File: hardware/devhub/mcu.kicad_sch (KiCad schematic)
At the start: 18 parts, among them J4 SWD, J9 UART debug, U3 STM32G0B1RET6

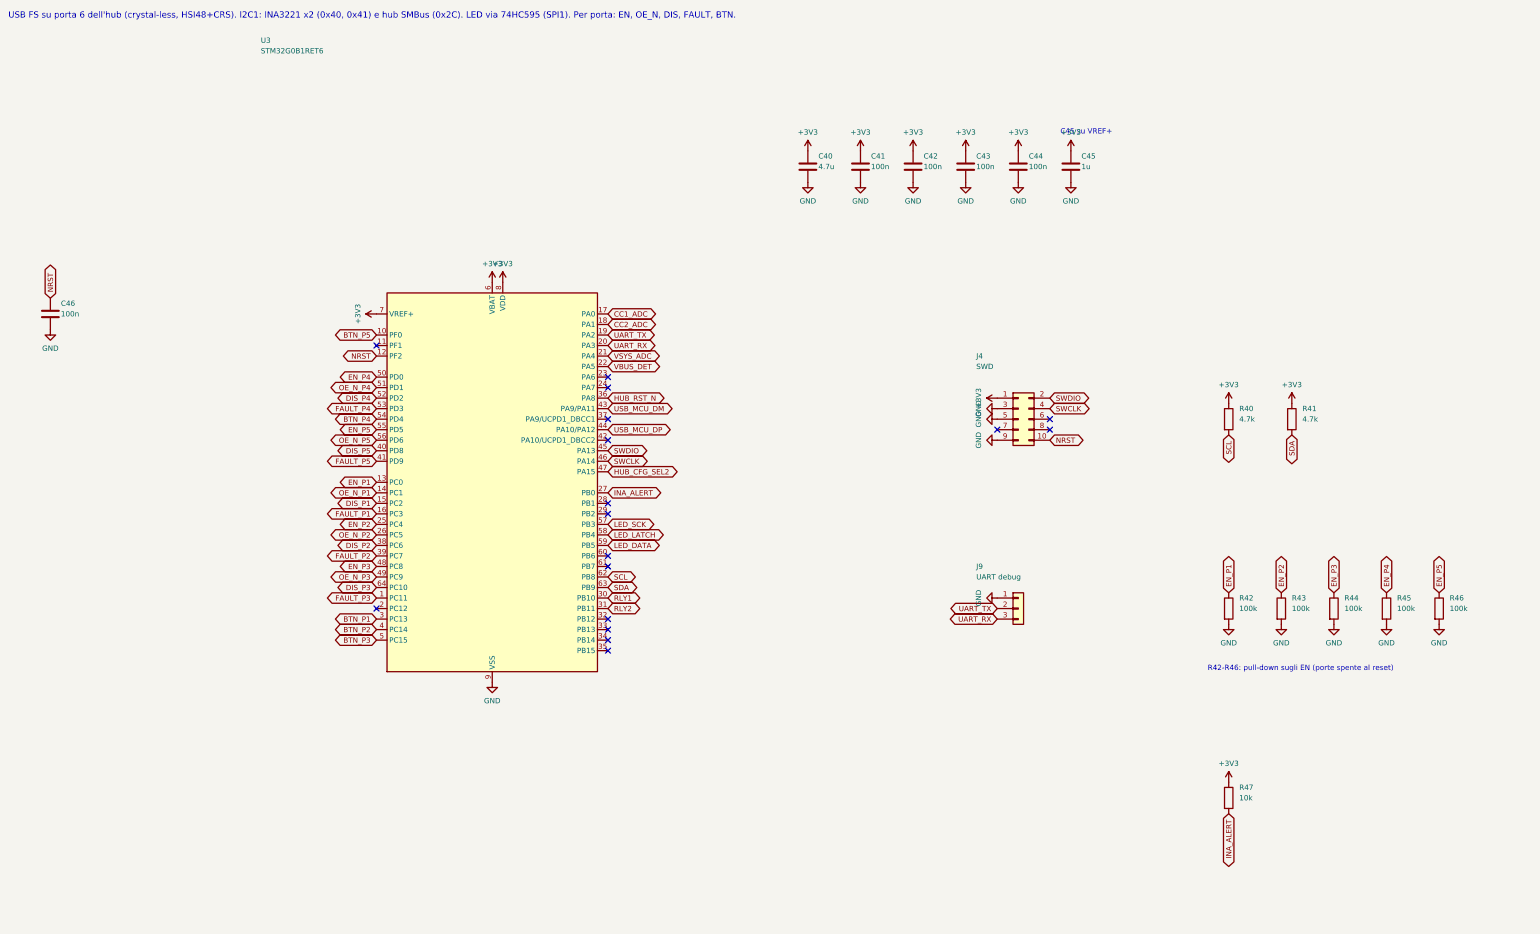
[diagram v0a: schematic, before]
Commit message: Schematic v0.2: hub reset supervisor, 1 A LDO, reorganized sheets, USB connectors and crystal
Functional changes:
- USB2517 RESET_N with pull-up and MCP120T-300 supervisor, wired-OR with
  the MCU (open-drain): resetting the MCU no longer resets the hub, so the
  ST DFU bootloader is reachable through it (D16/D17).
- 3.3 V LDO: AP7361C-33E (1 A, SOT-223) instead of AP2112K, which
  dissipated too much with the hub load.
- 74HC595 /OE on PB6 with pull-up: LEDs off until firmware enables them.
- Orange D93 instead of blue, USB-A bulk capacitance >= 120 uF, relay coil
  pinout fixed, snubbers marked DNP, Cliff FCR7350 banana jack footprints.
- D18: horizontal USB connectors, GCT USB4105-GF-A (USB-C) and Kycon
  KUSBX-AS1N-B (USB-A).
- D19: YXC X322524MOB4SI 24 MHz crystal (C_L 12 pF), 15 pF C0G load caps.

Layout: nearby parts wired directly, every net still explicitly named;
local labels inside sheets, global only across sheets, hierarchical for
ports. Files saved with KiCad 10.

Connectivity checked against the previous netlist, ERC clean.
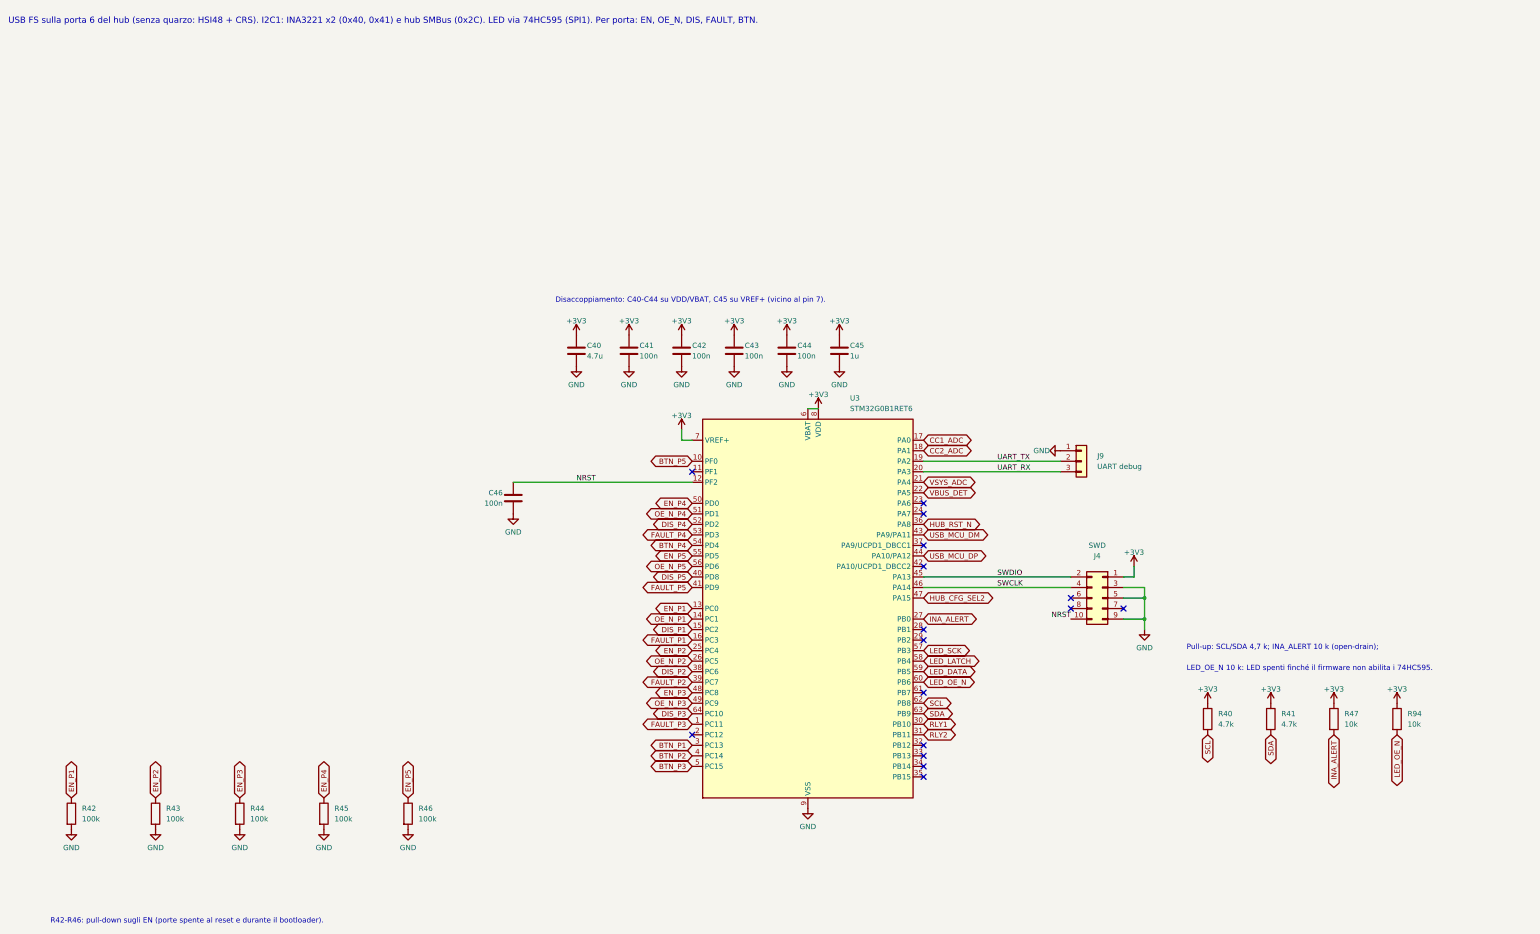
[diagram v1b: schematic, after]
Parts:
- added R94: 10k, Resistor_SMD:R_0603_1608Metric, symbol Device:R
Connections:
- net +3V3: now also R94.1
- net LED_OE_N: now reaches U3.60 (PB6)
- net LED_OE_N: now also R94.2
- no-connect marks 17 -> 16
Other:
- note added: "Disaccoppiamento: C40-C44 su VDD/VBAT, C45 su VREF+ (vicino al pin 7)."
- note added: "LED_OE_N 10 k: LED spenti finché il firmware non abilita i 74HC595."
- note added: "Pull-up: SCL/SDA 4,7 k; INA_ALERT 10 k (open-drain);"
- note added: "R42-R46: pull-down sugli EN (porte spente al reset e durante il bootloader)."
- note added: "USB FS sulla porta 6 del hub (senza quarzo: HSI48 + CRS). I2C1: INA3221 x2 (0x40, 0x41) e hub SMBus (0x2C). LED via 74HC595 (SPI1). Per porta: EN, OE_N, DIS, FAULT, BTN."
- note removed: "C45 su VREF+"
- note removed: "R42-R46: pull-down sugli EN (porte spente al reset)"
- note removed: "USB FS su porta 6 dell'hub (crystal-less, HSI48+CRS). I2C1: INA3221 x2 (0x40, 0x41) e hub SMBus (0x2C). LED via 74HC595 (SPI1). Per porta: EN, OE_N, DIS, FAULT, BTN."

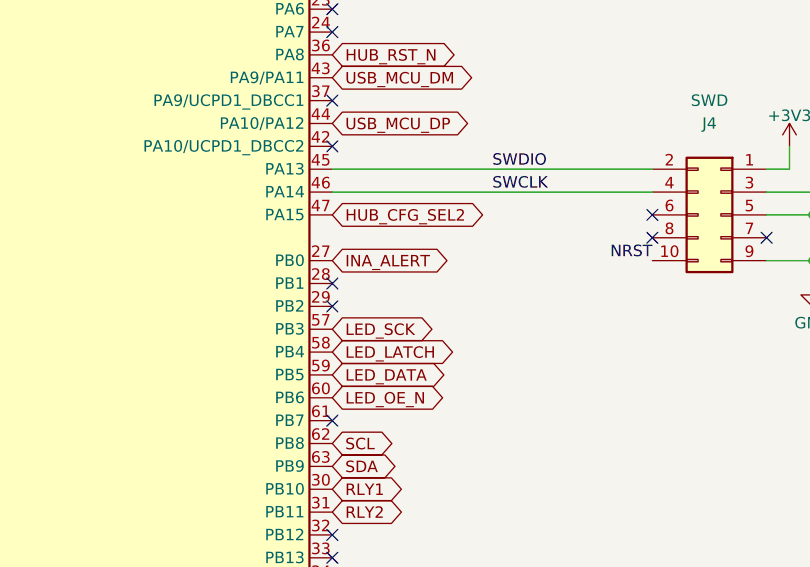
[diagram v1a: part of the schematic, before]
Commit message: Lab-use protection: TPS259470A input eFuse, PI3USB4002A data switches; AGENTS.md
Power input (D20, D21):
- TPS259470A eFuse after the shunt: trips above 5.84 V and below 4.0 V,
  zener on EN to withstand up to 28 V, 3.5 A limit, ~5 ms soft start,
  auto-retry, FLT to the MCU on PB1.
- The shunt stays before the eFuse, so the INA3221 still measures the input
  voltage when the eFuse is off.

Ports (D22): PI3USB4002A instead of TS3USB30E. The connector side withstands
24 V and opens above 4.75 V, so a D+/D- short to VBUS on a board under test
no longer reaches the 3.3 V rail.

Symbols for both ICs added to the project library. AGENTS.md added: the
schematic is edited in KiCad or with targeted changes, never regenerated by
script. Sheets re-saved by KiCad.

Connectivity checked against the previous netlist, ERC clean.
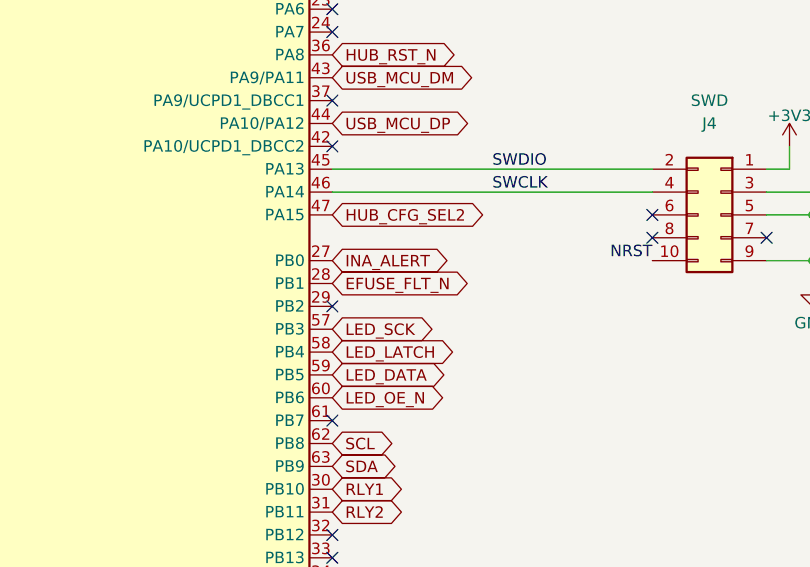
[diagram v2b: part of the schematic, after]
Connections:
- net EFUSE_FLT_N: now reaches U3.28 (PB1)
- no-connect marks 16 -> 15
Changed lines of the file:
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@@
 	)
 	(no_connect
-		(at 231.14 162.56)
-	)
-	(no_connect
 		(at 231.14 190.5)
 	)
@@
 		)
 	)
+	(global_label "EFUSE_FLT_N"
+		(shape bidirectional)
+		(at 231.14 162.56 0)
+		(fields_autoplaced yes)
+		(effects
+			(font
+				(size 1.27 1.27)
+			)
+			(justify left)
+		)
+		(property "Intersheetrefs" "${INTERSHEET_REFS}"
+			(at 231.14 162.56 0)
+			(hide yes)
+			(show_name no)
+			(do_not_autoplace no)
+			(effects
+				(font
+					(size 1.27 1.27)
+				)
+			)
+		)
+	)
 	(global_label "DIS_P5"
 		(shape bidirectional)
@@
 		(in_pos_files yes)
 		(dnp no)
-		(property "Reference" "#PWR074"
+		(property "Reference" "#PWR082"
 			(at 205.74 109.22 0)
 			(hide yes)
@@
 			(project "devhub"
 				(path "/af6ea7d8-d1ba-5fc6-aec8-abf514847630/357eb134-3b36-5717-b194-1b0e8ceb4547"
-					(reference "#PWR074")
+					(reference "#PWR082")
 					(unit 1)
 				)
@@
 		(in_pos_files yes)
 		(dnp no)
-		(property "Reference" "#PWR097"
+		(property "Reference" "#PWR105"
 			(at 45.72 210.82 0)
 			(hide yes)
@@
 			(project "devhub"
 				(path "/af6ea7d8-d1ba-5fc6-aec8-abf514847630/357eb134-3b36-5717-b194-1b0e8ceb4547"
-					(reference "#PWR097")
+					(reference "#PWR105")
 					(unit 1)
 				)
@@
 		(in_pos_files yes)
 		(dnp no)
-		(property "Reference" "#PWR073"
+		(property "Reference" "#PWR081"
 			(at 203.2 205.74 0)
 			(hide yes)
@@
 			(project "devhub"
 				(path "/af6ea7d8-d1ba-5fc6-aec8-abf514847630/357eb134-3b36-5717-b194-1b0e8ceb4547"
-					(reference "#PWR073")
+					(reference "#PWR081")
 					(unit 1)
 				)
@@
 		(in_pos_files yes)
 		(dnp no)
-		(property "Reference" "#PWR080"
+		(property "Reference" "#PWR088"
 			(at 172.72 91.44 0)
 			(hide yes)
@@
 			(project "devhub"
 				(path "/af6ea7d8-d1ba-5fc6-aec8-abf514847630/357eb134-3b36-5717-b194-1b0e8ceb4547"
-					(reference "#PWR080")
+					(reference "#PWR088")
 					(unit 1)
 				)
@@
 		(in_pos_files yes)
 		(dnp no)
-		(property "Reference" "#PWR096"
+		(property "Reference" "#PWR104"
 			(at 25.4 210.82 0)
 			(hide yes)
@@
 			(project "devhub"
 				(path "/af6ea7d8-d1ba-5fc6-aec8-abf514847630/357eb134-3b36-5717-b194-1b0e8ceb4547"
-					(reference "#PWR096")
+					(reference "#PWR104")
 					(unit 1)
 				)
@@
 		(in_pos_files yes)
 		(dnp no)
-		(property "Reference" "#PWR089"
+		(property "Reference" "#PWR097"
 			(at 264.16 119.38 0)
 			(hide yes)
@@
 			(project "devhub"
 				(path "/af6ea7d8-d1ba-5fc6-aec8-abf514847630/357eb134-3b36-5717-b194-1b0e8ceb4547"
-					(reference "#PWR089")
+					(reference "#PWR097")
 					(unit 1)
 				)
@@
 		(in_pos_files yes)
 		(dnp no)
-		(property "Reference" "#PWR090"
+		(property "Reference" "#PWR098"
 			(at 281.94 147.32 0)
 			(hide yes)
@@
 			(project "devhub"
 				(path "/af6ea7d8-d1ba-5fc6-aec8-abf514847630/357eb134-3b36-5717-b194-1b0e8ceb4547"
-					(reference "#PWR090")
+					(reference "#PWR098")
 					(unit 1)
 				)
@@
 		(in_pos_files yes)
 		(dnp no)
-		(property "Reference" "#PWR083"
+		(property "Reference" "#PWR091"
 			(at 185.42 99.06 0)
 			(hide yes)
@@
 			(project "devhub"
 				(path "/af6ea7d8-d1ba-5fc6-aec8-abf514847630/357eb134-3b36-5717-b194-1b0e8ceb4547"
-					(reference "#PWR083")
+					(reference "#PWR091")
 					(unit 1)
 				)
@@
 		(in_pos_files yes)
 		(dnp no)
-		(property "Reference" "#PWR085"
+		(property "Reference" "#PWR093"
 			(at 198.12 99.06 0)
 			(hide yes)
@@
 			(project "devhub"
 				(path "/af6ea7d8-d1ba-5fc6-aec8-abf514847630/357eb134-3b36-5717-b194-1b0e8ceb4547"
-					(reference "#PWR085")
+					(reference "#PWR093")
 					(unit 1)
 				)
@@
 		(in_pos_files yes)
 		(dnp no)
-		(property "Reference" "#PWR077"
+		(property "Reference" "#PWR085"
 			(at 147.32 99.06 0)
 			(hide yes)
@@
 			(project "devhub"
 				(path "/af6ea7d8-d1ba-5fc6-aec8-abf514847630/357eb134-3b36-5717-b194-1b0e8ceb4547"
-					(reference "#PWR077")
+					(reference "#PWR085")
 					(unit 1)
 				)
@@
 		(in_pos_files yes)
 		(dnp no)
-		(property "Reference" "#PWR098"
+		(property "Reference" "#PWR106"
 			(at 66.04 210.82 0)
 			(hide yes)
@@
 			(project "devhub"
 				(path "/af6ea7d8-d1ba-5fc6-aec8-abf514847630/357eb134-3b36-5717-b194-1b0e8ceb4547"
-					(reference "#PWR098")
+					(reference "#PWR106")
 					(unit 1)
 				)
@@
 		(in_pos_files yes)
 		(dnp no)
-		(property "Reference" "#PWR082"
+		(property "Reference" "#PWR090"
 			(at 185.42 91.44 0)
 			(hide yes)
@@
 			(project "devhub"
 				(path "/af6ea7d8-d1ba-5fc6-aec8-abf514847630/357eb134-3b36-5717-b194-1b0e8ceb4547"
-					(reference "#PWR082")
+					(reference "#PWR090")
 					(unit 1)
 				)
@@
 		(in_pos_files yes)
 		(dnp no)
-		(property "Reference" "#PWR087"
+		(property "Reference" "#PWR095"
 			(at 210.82 99.06 0)
 			(hide yes)
@@
 			(project "devhub"
 				(path "/af6ea7d8-d1ba-5fc6-aec8-abf514847630/357eb134-3b36-5717-b194-1b0e8ceb4547"
-					(reference "#PWR087")
+					(reference "#PWR095")
 					(unit 1)
 				)
@@
 		(in_pos_files yes)
 		(dnp no)
-		(property "Reference" "#PWR084"
+		(property "Reference" "#PWR092"
 			(at 198.12 91.44 0)
 			(hide yes)
@@
 			(project "devhub"
 				(path "/af6ea7d8-d1ba-5fc6-aec8-abf514847630/357eb134-3b36-5717-b194-1b0e8ceb4547"
-					(reference "#PWR084")
+					(reference "#PWR092")
 					(unit 1)
 				)
@@
 		(in_pos_files yes)
 		(dnp no)
-		(property "Reference" "#PWR100"
+		(property "Reference" "#PWR108"
 			(at 106.68 210.82 0)
 			(hide yes)
@@
 			(project "devhub"
 				(path "/af6ea7d8-d1ba-5fc6-aec8-abf514847630/357eb134-3b36-5717-b194-1b0e8ceb4547"
-					(reference "#PWR100")
+					(reference "#PWR108")
 					(unit 1)
 				)
@@
 		(in_pos_files yes)
 		(dnp no)
-		(property "Reference" "#PWR086"
+		(property "Reference" "#PWR094"
 			(at 210.82 91.44 0)
 			(hide yes)
@@
 			(project "devhub"
 				(path "/af6ea7d8-d1ba-5fc6-aec8-abf514847630/357eb134-3b36-5717-b194-1b0e8ceb4547"
-					(reference "#PWR086")
+					(reference "#PWR094")
 					(unit 1)
 				)
@@
 		(in_pos_files yes)
 		(dnp no)
-		(property "Reference" "#PWR099"
+		(property "Reference" "#PWR107"
 			(at 86.36 210.82 0)
 			(hide yes)
@@
 			(project "devhub"
 				(path "/af6ea7d8-d1ba-5fc6-aec8-abf514847630/357eb134-3b36-5717-b194-1b0e8ceb4547"
-					(reference "#PWR099")
+					(reference "#PWR107")
 					(unit 1)
 				)
@@
 		(in_pos_files yes)
 		(dnp no)
-		(property "Reference" "#PWR079"
+		(property "Reference" "#PWR087"
 			(at 160.02 99.06 0)
 			(hide yes)
@@
 			(project "devhub"
 				(path "/af6ea7d8-d1ba-5fc6-aec8-abf514847630/357eb134-3b36-5717-b194-1b0e8ceb4547"
-					(reference "#PWR079")
+					(reference "#PWR087")
 					(unit 1)
 				)
@@
 		(in_pos_files yes)
 		(dnp no)
-		(property "Reference" "#PWR092"
+		(property "Reference" "#PWR100"
 			(at 299.72 180.34 0)
 			(hide yes)
@@
 			(project "devhub"
 				(path "/af6ea7d8-d1ba-5fc6-aec8-abf514847630/357eb134-3b36-5717-b194-1b0e8ceb4547"
-					(reference "#PWR092")
+					(reference "#PWR100")
 					(unit 1)
 				)
@@
 		(in_pos_files yes)
 		(dnp no)
-		(property "Reference" "#PWR088"
+		(property "Reference" "#PWR096"
 			(at 132.08 134.62 0)
 			(hide yes)
@@
 			(project "devhub"
 				(path "/af6ea7d8-d1ba-5fc6-aec8-abf514847630/357eb134-3b36-5717-b194-1b0e8ceb4547"
-					(reference "#PWR088")
+					(reference "#PWR096")
 					(unit 1)
 				)
@@
 		(in_pos_files yes)
 		(dnp no)
-		(property "Reference" "#PWR075"
+		(property "Reference" "#PWR083"
 			(at 172.72 114.3 0)
 			(hide yes)
@@
 			(project "devhub"
 				(path "/af6ea7d8-d1ba-5fc6-aec8-abf514847630/357eb134-3b36-5717-b194-1b0e8ceb4547"
-					(reference "#PWR075")
+					(reference "#PWR083")
 					(unit 1)
 				)
@@
 		(in_pos_files yes)
 		(dnp no)
-		(property "Reference" "#PWR078"
+		(property "Reference" "#PWR086"
 			(at 160.02 91.44 0)
 			(hide yes)
@@
 			(project "devhub"
 				(path "/af6ea7d8-d1ba-5fc6-aec8-abf514847630/357eb134-3b36-5717-b194-1b0e8ceb4547"
-					(reference "#PWR078")
+					(reference "#PWR086")
 					(unit 1)
 				)
@@
 		(in_pos_files yes)
 		(dnp no)
-		(property "Reference" "#PWR076"
+		(property "Reference" "#PWR084"
 			(at 147.32 91.44 0)
 			(hide yes)
@@
 			(project "devhub"
 				(path "/af6ea7d8-d1ba-5fc6-aec8-abf514847630/357eb134-3b36-5717-b194-1b0e8ceb4547"
-					(reference "#PWR076")
+					(reference "#PWR084")
 					(unit 1)
 				)
@@
 		(in_pos_files yes)
 		(dnp no)
-		(property "Reference" "#PWR081"
+		(property "Reference" "#PWR089"
 			(at 172.72 99.06 0)
 			(hide yes)
@@
 			(project "devhub"
 				(path "/af6ea7d8-d1ba-5fc6-aec8-abf514847630/357eb134-3b36-5717-b194-1b0e8ceb4547"
-					(reference "#PWR081")
+					(reference "#PWR089")
 					(unit 1)
 				)
@@
 		(in_pos_files yes)
 		(dnp no)
-		(property "Reference" "#PWR095"
+		(property "Reference" "#PWR103"
 			(at 345.44 180.34 0)
 			(hide yes)
@@
 			(project "devhub"
 				(path "/af6ea7d8-d1ba-5fc6-aec8-abf514847630/357eb134-3b36-5717-b194-1b0e8ceb4547"
-					(reference "#PWR095")
+					(reference "#PWR103")
 					(unit 1)
 				)
@@
 		(in_pos_files yes)
 		(dnp no)
-		(property "Reference" "#PWR094"
+		(property "Reference" "#PWR102"
 			(at 330.2 180.34 0)
 			(hide yes)
@@
 			(project "devhub"
 				(path "/af6ea7d8-d1ba-5fc6-aec8-abf514847630/357eb134-3b36-5717-b194-1b0e8ceb4547"
-					(reference "#PWR094")
+					(reference "#PWR102")
 					(unit 1)
 				)
@@
 		(in_pos_files yes)
 		(dnp no)
-		(property "Reference" "#PWR091"
+		(property "Reference" "#PWR099"
 			(at 284.48 162.56 0)
 			(hide yes)
@@
 			(project "devhub"
 				(path "/af6ea7d8-d1ba-5fc6-aec8-abf514847630/357eb134-3b36-5717-b194-1b0e8ceb4547"
-					(reference "#PWR091")
+					(reference "#PWR099")
 					(unit 1)
 				)
@@
 		(in_pos_files yes)
 		(dnp no)
-		(property "Reference" "#PWR093"
+		(property "Reference" "#PWR101"
 			(at 314.96 180.34 0)
 			(hide yes)
@@
 			(project "devhub"
 				(path "/af6ea7d8-d1ba-5fc6-aec8-abf514847630/357eb134-3b36-5717-b194-1b0e8ceb4547"
-					(reference "#PWR093")
+					(reference "#PWR101")
 					(unit 1)
 				)
